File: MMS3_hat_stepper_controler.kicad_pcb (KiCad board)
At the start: 4 copper layers, 100 x 50 mm, 94 parts, among them J1 Chainbus in, J2 Chainbus Out, J3 Conn_01x04_Pin, J4 AMASS XT60 Male, J5 AMASS XT60 Female, J6 Encoder connector, J7 Motor connector, J8 Conn_01x03_Pin, SW1 SW_DIP_x04, U1 SN74CB3Q3384APW, U2 M24C64, U3 TMC5130A-TA, U4 AMS1117, U5 LM2596HVS-ADJRG

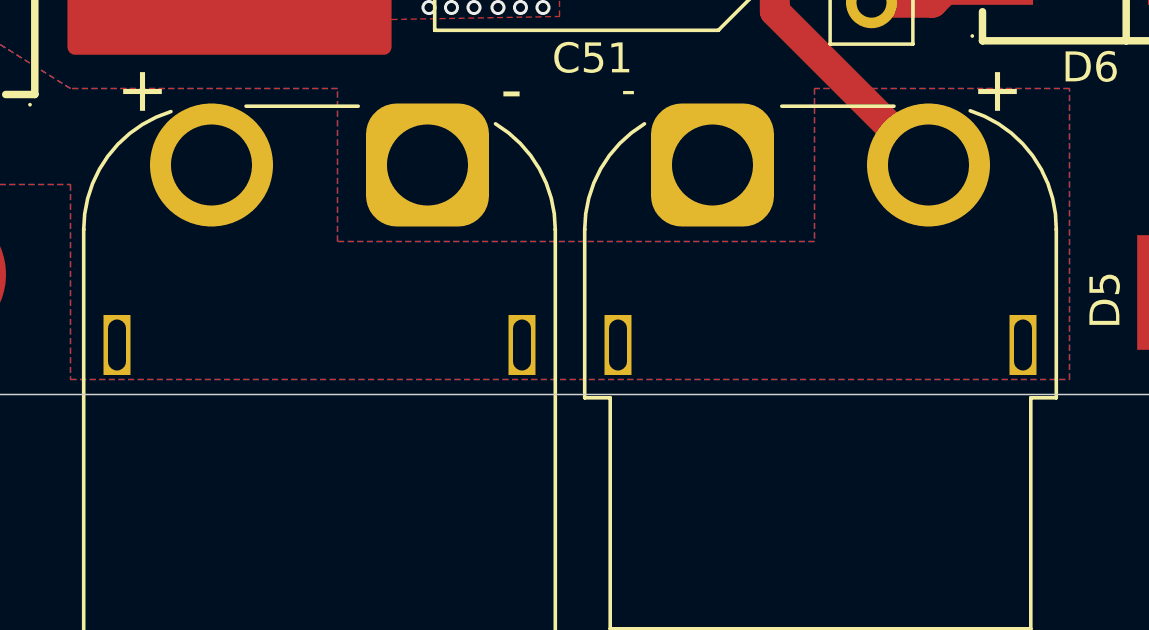
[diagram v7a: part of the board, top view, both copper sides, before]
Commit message: added more vias to XT60
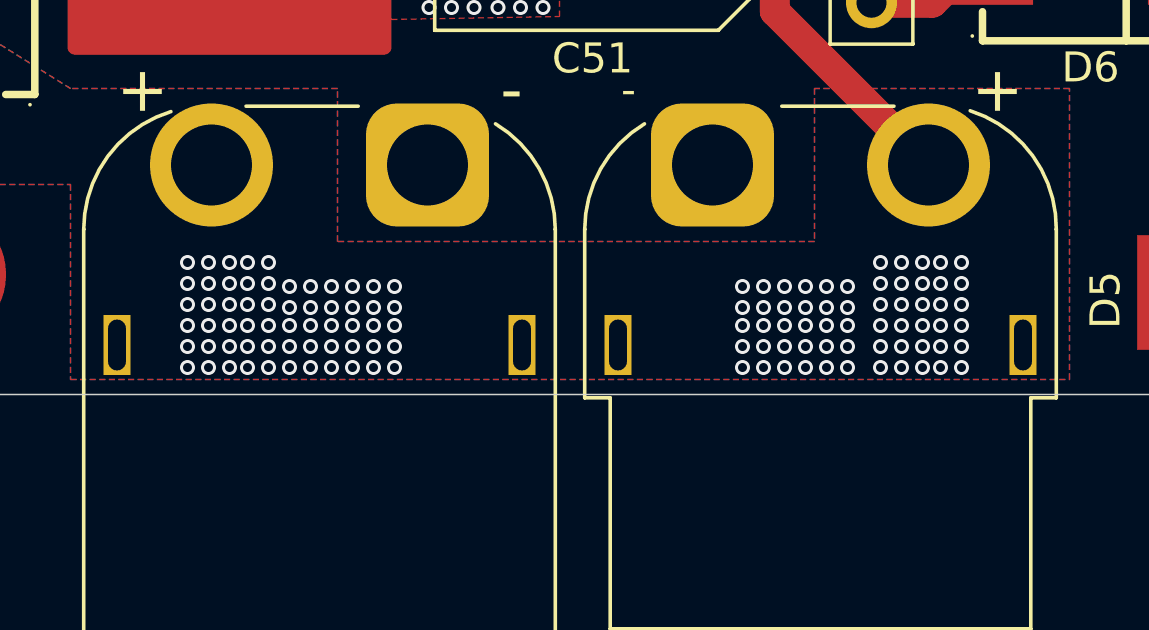
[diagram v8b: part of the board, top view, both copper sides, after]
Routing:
- net Vin: vias 0 -> 120
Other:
- board text added: "MMS3 Hat Stepper Version 1.0 Made by Wojciech Szafrański"
- board text removed: "Version 1.0 Made by Wojciech Szafrański"
